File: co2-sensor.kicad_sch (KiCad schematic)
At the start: 20 parts, among them J1 Waveshare E-Ink, Q1 Si1308EDL

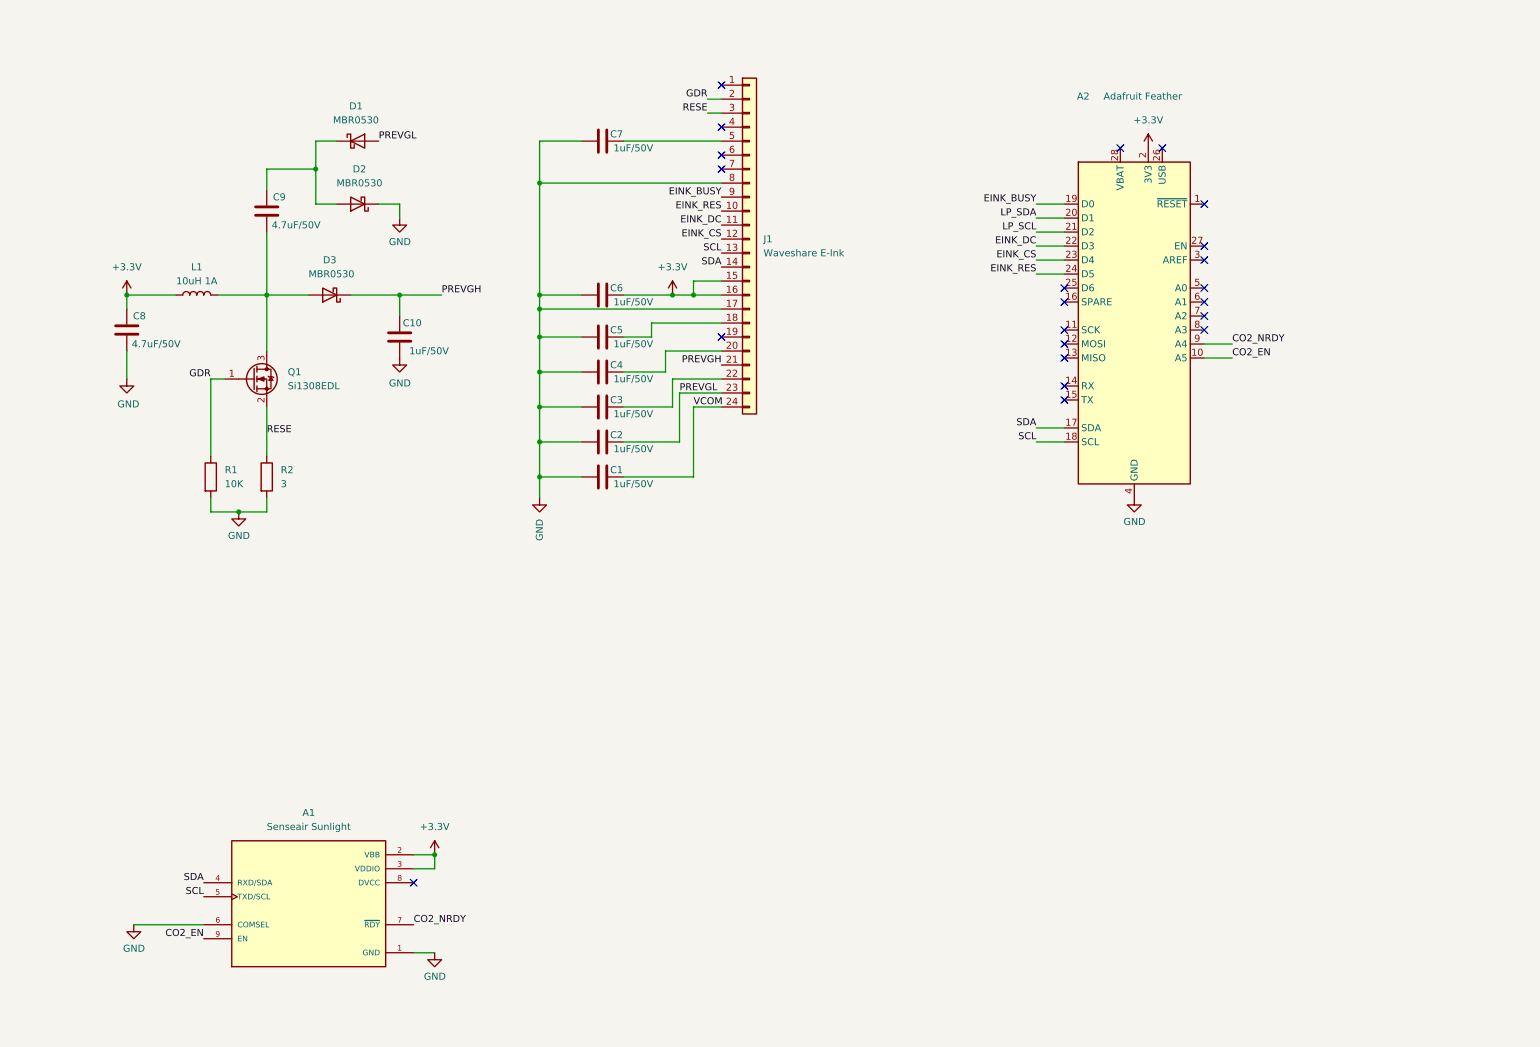
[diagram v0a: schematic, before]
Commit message: Rework to use ESP32 module directly
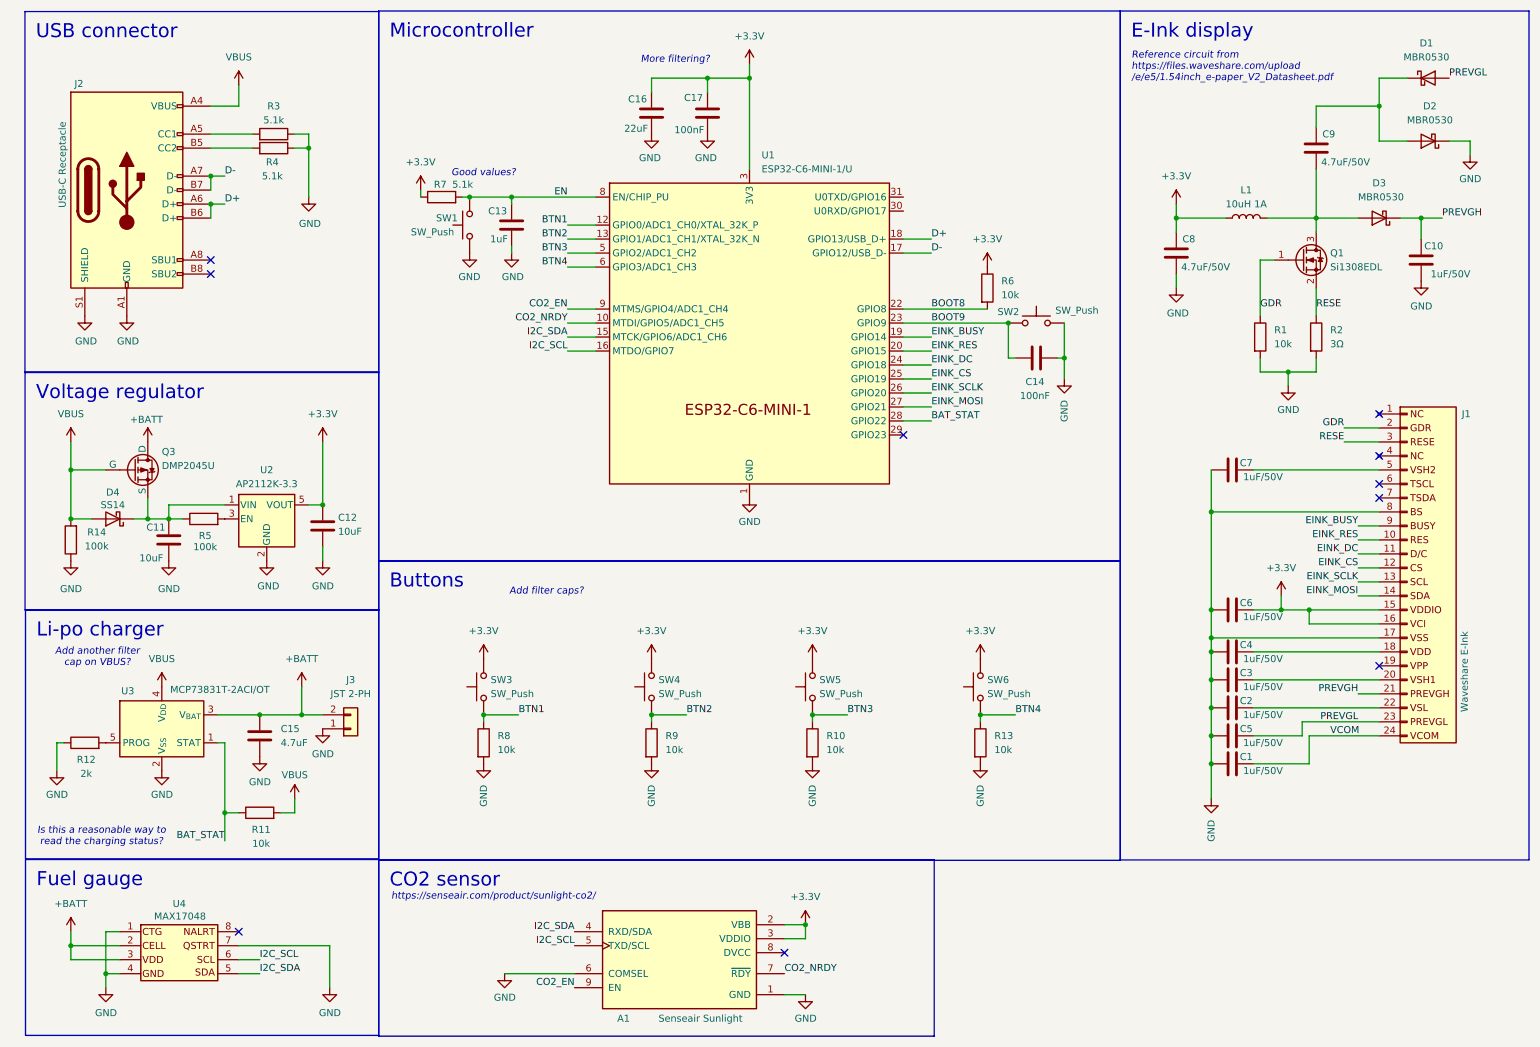
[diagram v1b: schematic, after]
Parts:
- removed A2: Adafruit Feather, Module:Adafruit_Feather, symbol MCU_Module:Adafruit_Feather_Generic
- added C11, C12: 10uF, Capacitor_SMD:C_0805_2012Metric, symbol Device:C
- added C13: 1uF, Capacitor_SMD:C_0805_2012Metric, symbol Device:C
- added C14, C17: 100nF, Capacitor_SMD:C_0805_2012Metric, symbol Device:C
- added C15: 4.7uF, Capacitor_SMD:C_0805_2012Metric, symbol Device:C
- added C16: 22uF, Capacitor_SMD:C_0805_2012Metric, symbol Device:C
- added D4: SS14, Diode_SMD:D_SOD-123, symbol Diode:MBR0540
- added J2: USB-C Receptacle, Connector_USB:USB_C_Receptacle_G-Switch_GT-USB-7010ASV, symbol Connector:USB_C_Receptacle_USB2.0_16P
- added J3: JST 2-PH, Connector_JST:JST_PH_S2B-PH-SM4-TB_1x02-1MP_P2.00mm_Horizontal, symbol Connector_Generic:Conn_01x02
- added Q3: DMP2045U, Package_TO_SOT_SMD:SOT-23, symbol Simulation_SPICE:PMOS
- added R10, R11, R13, R6, R8, R9: 10k, Capacitor_SMD:C_0805_2012Metric, symbol Device:R
- added R12: 2k, Capacitor_SMD:C_0805_2012Metric, symbol Device:R
- added R14, R5: 100k, Capacitor_SMD:C_0805_2012Metric, symbol Device:R
- added R3, R4, R7: 5.1k, Capacitor_SMD:C_0805_2012Metric, symbol Device:R
- added SW1, SW2, SW3, SW4, SW5, SW6: SW_Push, Button_Switch_SMD:SW_SPST_SKQG_WithStem, symbol Switch:SW_Push
- added U1: ESP32-C6-MINI-1/U, PCM_Espressif:ESP32-C6-MINI-1, symbol PCM_Espressif:ESP32-C6-MINI-1/U
- added U2: AP2112K-3.3, Package_TO_SOT_SMD:SOT-23-5, symbol Regulator_Linear:AP2112K-3.3
- added U3: MCP73831T-2ACI/OT, Package_TO_SOT_SMD:SOT-23-5, symbol Battery_Management:MCP73831-2-OT
- added U4: MAX17048, Package_DFN_QFN:DFN-8-1EP_2x2mm_P0.5mm_EP1.05x1.75mm, symbol Connector_Generic:Conn_02x04_Counter_Clockwise
- R1: value 10K -> 10k
- R2: value 3 -> 3Ω
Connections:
- net +3.3V: now also C12.1, C16.2, C17.2, R6.1, R7.1, SW3.2, SW4.2, SW5.2, SW6.2, U1.3 (3V3), U2.5 (VOUT)
- net CO2_EN: now also U1.9 (MTMS/GPIO4/ADC1_CH4)
- net CO2_NRDY: now also U1.10 (MTDI/GPIO5/ADC1_CH5)
- net EINK_BUSY: now also U1.19 (GPIO14)
- net EINK_CS: now also U1.25 (GPIO19)
- net EINK_DC: now also U1.24 (GPIO18)
- net EINK_RES: now also U1.20 (GPIO15)
- net GND: now also C11.2, C12.2, C13.1, C14.1, C15.2, C16.1, C17.1, J2.A1 (GND), J2.A12 (GND), J2.B1 (GND), J2.B12 (GND), J2.S1 (SHIELD), J3.1 (Pin_1), R10.2, R12.1, R13.2, R14.1, R3.1, R4.1, R8.2, R9.2, SW1.1, SW2.1, U1.1 (GND), U2.2 (GND), U3.2 (V_{SS}), U4.1 (Pin_1), U4.4 (Pin_4), U4.7 (Pin_7)
- net PREVGL: now also C5.2; no longer C2.2
- net at C4.2: now also J1.18 (Pin_18); no longer J1.20 (Pin_20)
- net at C3.2: now also J1.20 (Pin_20); no longer J1.22 (Pin_22)
- net SCL renamed EINK_SCLK
- net EINK_SCLK: now also U1.26 (GPIO20); no longer A1.5 (TXD/SCL)
- net SDA renamed EINK_MOSI
- net EINK_MOSI: now also U1.27 (GPIO21); no longer A1.4 (RXD/SDA)
- new net: C11.1, D4.1 (K), Q3.3 (S), R5.1, U2.1 (VIN)
- new net: U1.11 (GND), U1.14 (GND), U1.2 (GND), U1.36 (GND), U1.37 (GND), U1.38 (GND), U1.39 (GND), U1.40 (GND), U1.41 (GND), U1.42 (GND), U1.43 (GND), U1.44 (GND), U1.45 (GND), U1.46 (GND), U1.47 (GND), U1.48 (GND), U1.49 (GND), U1.50 (GND), U1.51 (GND), U1.52 (GND), U1.53 (GND)
- new net: J2.A5 (CC1), R3.2
- new net: J2.B5 (CC2), R4.2
- new net: C2.2, J1.22 (Pin_22)
- new net: R5.2, U2.3 (EN)
- new net: R12.2, U3.5 (PROG)
- new net +BATT: C15.1, J3.2 (Pin_2), Q3.1 (D), U3.3 (V_{BAT}), U4.2 (Pin_2), U4.3 (Pin_3)
- new net BAT_STAT: R11.1, U1.28 (GPIO22), U3.1 (STAT)
- new net BOOT8: R6.2, U1.22 (GPIO8)
- new net BOOT9: C14.2, SW2.2, U1.23 (GPIO9)
- new net BTN1: R8.1, SW3.1, U1.12 (GPIO0/ADC1_CH0/XTAL_32K_P)
- new net BTN2: R9.1, SW4.1, U1.13 (GPIO1/ADC1_CH1/XTAL_32K_N)
- new net BTN3: R10.1, SW5.1, U1.5 (GPIO2/ADC1_CH2)
- new net BTN4: R13.1, SW6.1, U1.6 (GPIO3/ADC1_CH3)
- new net D+: J2.A6 (D+), J2.B6 (D+), U1.18 (GPIO13/USB_D+)
- new net D-: J2.A7 (D-), J2.B7 (D-), U1.17 (GPIO12/USB_D-)
- new net EN: C13.2, R7.2, SW1.2, U1.8 (EN/CHIP_PU)
- new net I2C_SCL: A1.5 (TXD/SCL), U1.16 (MTDO/GPIO7), U4.6 (Pin_6)
- new net I2C_SDA: A1.4 (RXD/SDA), U1.15 (MTCK/GPIO6/ADC1_CH6), U4.5 (Pin_5)
- new net VBUS: D4.2 (A), J2.A4 (VBUS), J2.A9 (VBUS), J2.B4 (VBUS), J2.B9 (VBUS), Q3.2 (G), R11.2, R14.2, U3.4 (V_{DD})
- no-connect marks 22 -> 10
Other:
- note added: "Add another filter cap on VBUS?"
- note added: "Add filter caps?"
- note added: "Good values?"
- note added: "Is this a reasonable way to read the charging status?"
- note added: "More filtering?"
- note added: "Reference circuit from https://files.waveshare.com/upload /e/e5/1.54inch_e-paper_V2_Datasheet.pdf"
- note added: "https://senseair.com/product/sunlight-co2/"
- company: (none) -> blinry <mail@blinry.org>
- title: (none) -> Low-Power CO2 Sensor
- moved on the sheet: A1, C1, C10, C2, C3, C4, C6, C7, C8, C9, D1, D2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

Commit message: Polish before getting feedback
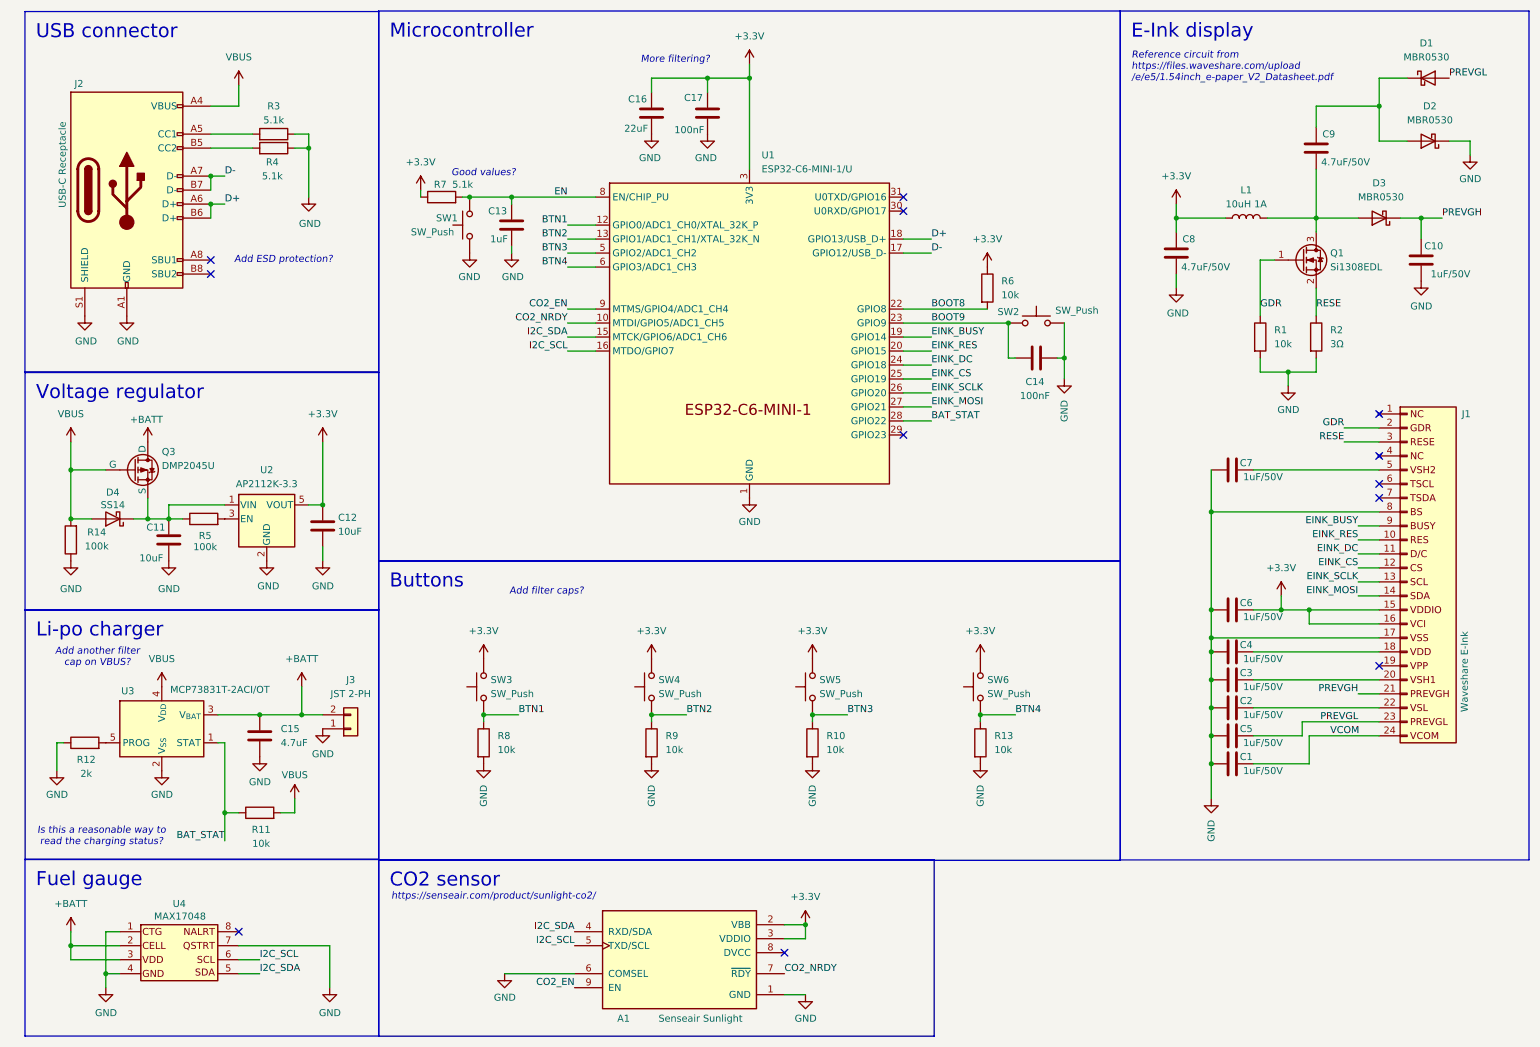
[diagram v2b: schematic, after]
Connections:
- net GND: now also U1.11 (GND), U1.14 (GND), U1.2 (GND), U1.36 (GND), U1.37 (GND), U1.38 (GND), U1.39 (GND), U1.40 (GND), U1.41 (GND), U1.42 (GND), U1.43 (GND), U1.44 (GND), U1.45 (GND), U1.46 (GND), U1.47 (GND), U1.48 (GND), U1.49 (GND), U1.50 (GND), U1.51 (GND), U1.52 (GND), U1.53 (GND)
- no-connect marks 10 -> 12
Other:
- note added: "Add ESD protection?"
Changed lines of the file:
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@@
+	)
+	(no_connect
+		(at 171.45 48.26)
 	)
 	(no_connect
@@
 		(at 45.72 59.69)
 	)
+	(no_connect
+		(at 171.45 45.72)
+	)
 	(wire
 		(pts
@@
 	(text_box "Fuel gauge"
 		(exclude_from_sim no)
-		(at 12.095 165.9646 0)
-		(size 64.105 31.9251)
+		(at 11.9966 165.9646 0)
+		(size 64.2034 32.0492)
 		(stroke
 			(width 0)
@@
 	(text_box "Li-po charger"
 		(exclude_from_sim no)
-		(at 12.095 120.65 0)
-		(size 64.105 45.2161)
+		(at 12.0233 120.65 0)
+		(size 64.1767 45.2649)
 		(stroke
 			(width 0)
@@
 		)
 	)
+	(text "Add ESD protection?"
+		(exclude_from_sim no)
+		(at 58.928 57.15 0)
+		(effects
+			(font
+				(size 1.27 1.27)
+				(italic yes)
+				(color 255 0 0 1)
+			)
+		)
+	)

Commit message: Add charging LED, make all wakeup sources trigger down
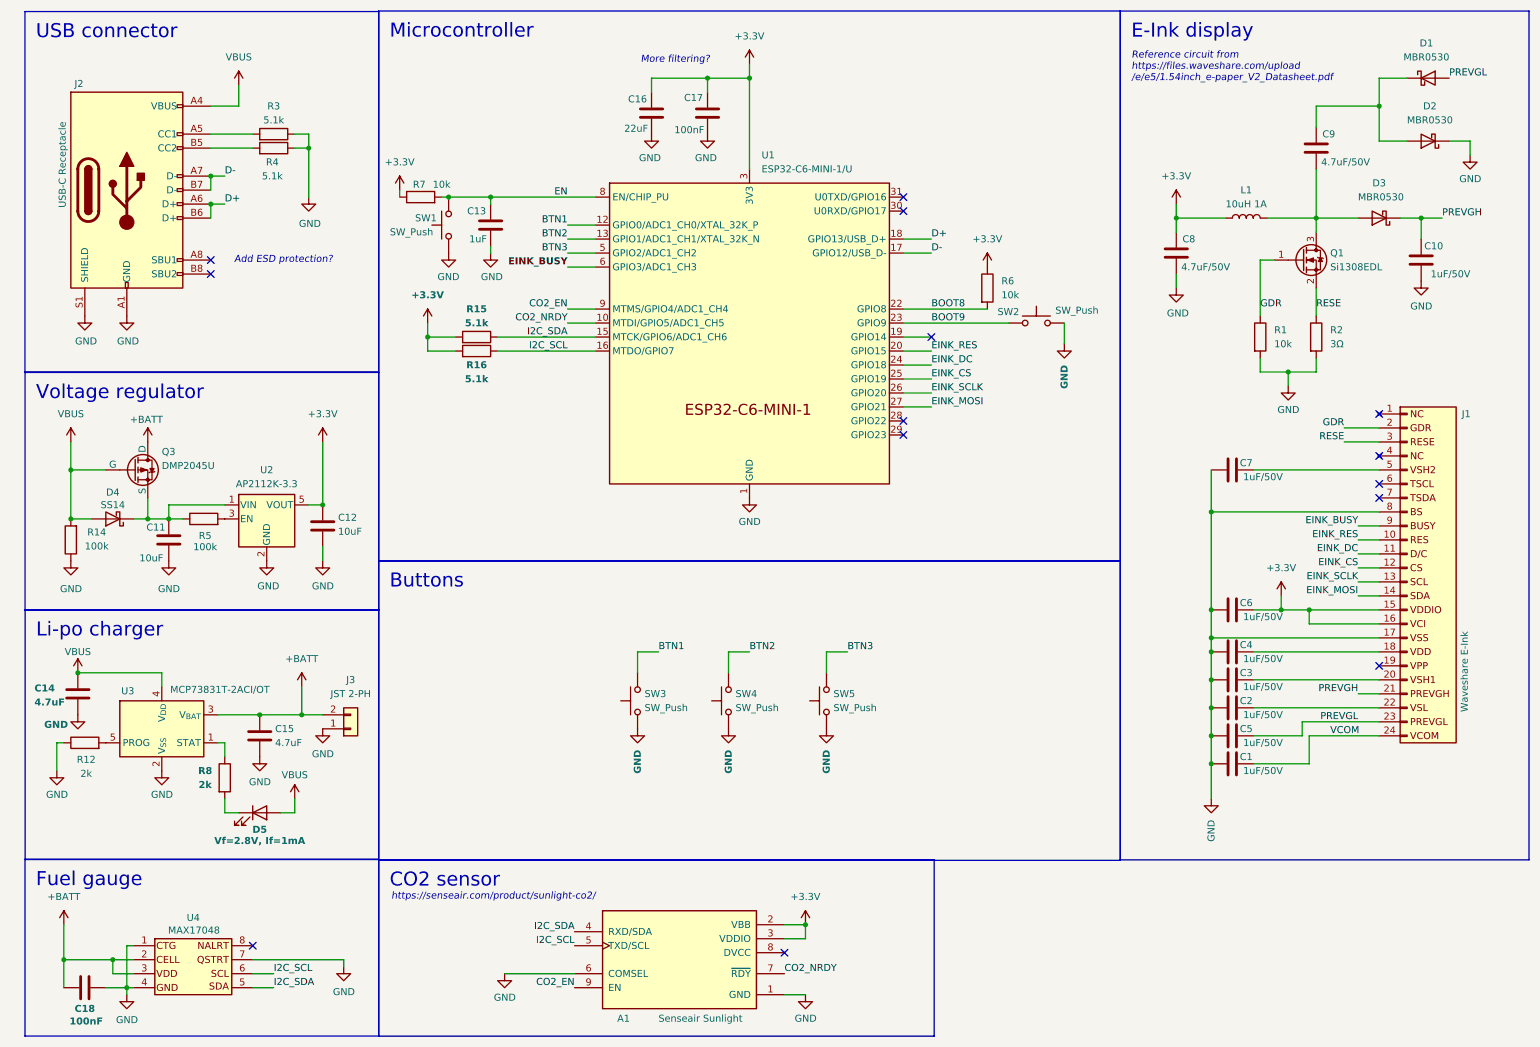
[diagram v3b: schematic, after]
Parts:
- removed R10, R11, R13, R9: 10k, Capacitor_SMD:C_0805_2012Metric, symbol Device:R
- removed SW6: SW_Push, Button_Switch_SMD:SW_SPST_SKQG_WithStem, symbol Switch:SW_Push
- added C18: 100nF, Capacitor_SMD:C_0805_2012Metric, symbol Device:C
- added D5: Vf=2.8V, If=1mA, LED_SMD:LED_0603_1608Metric, symbol Device:LED
- added R15, R16: 5.1k, Capacitor_SMD:C_0805_2012Metric, symbol Device:R
- C14: value 100nF -> 4.7uF
- R7: value 5.1k -> 10k
- R8: value 10k -> 2k
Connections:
- net BTN4 is gone; now on net EINK_BUSY: U1.6 (GPIO3/ADC1_CH3)
- net +3.3V: now also R15.2, R16.2; no longer SW3.2, SW4.2, SW5.2
- net +BATT: now also C18.2
- net BOOT9: no longer C14.2
- net BTN1: now also SW3.2; no longer R8.1, SW3.1
- net BTN2: now also SW4.2; no longer SW4.1
- net BTN3: now also SW5.2; no longer SW5.1
- net EINK_BUSY: no longer U1.19 (GPIO14)
- net GND: now also C14.2, SW3.1, SW4.1, SW5.1, C18.1; no longer C14.1, R8.2
- net I2C_SCL: now also R16.1
- net I2C_SDA: now also R15.1
- net VBUS: now also C14.1, D5.2 (A)
- net BAT_STAT: no longer names the net of U1.28 (GPIO22)
- net BAT_STAT: no longer U3.1 (STAT)
- new net: D5.1 (K), R8.2
- new net: R8.1, U3.1 (STAT)
- no-connect marks 12 -> 14
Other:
- note removed: "Add another filter cap on VBUS?"
- note removed: "Add filter caps?"
- note removed: "Good values?"
- note removed: "Is this a reasonable way to read the charging status?"
- moved on the sheet: C13, R7, SW1, U4

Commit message: Before manual de-bolding fix
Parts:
- removed D1, D2, D3: MBR0530, Diode_SMD:D_SOD-123, symbol Diode:MBR0530
- removed Q1: Si1308EDL, Package_TO_SOT_SMD:SOT-323_SC-70, symbol Transistor_FET:Si1308EDL
- added D1, D2, D6: SS14, Diode_SMD:D_SMA, symbol Diode:SS14
- added Q2: AO3400A, Package_TO_SOT_SMD:SOT-23, symbol Transistor_FET:AO3400A
- R2: value 3Ω -> 2Ω
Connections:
- net GDR: now also Q2.1 (G)
- net GND: now also D1.1 (K)
- net PREVGH: now also D2.1 (K)
- net PREVGL: now also D6.2 (A)
- net RESE: now also Q2.2 (S)
- net at C9.1, L1.2: now also D2.2 (A), Q2.3 (D)
- net at C9.2: now also D1.2 (A), D6.1 (K)
